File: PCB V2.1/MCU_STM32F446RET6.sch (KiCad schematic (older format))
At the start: 35 parts, among them J1 20021121-00010C4LF, J2 0475890001-MicroUSBPort, SW1 B3U-1000P, U1 STM32F446RET6_-_TQFP64, X1 ABM3B8.000MHZB2T, X2 ABS07-32.768KHZ-9-T

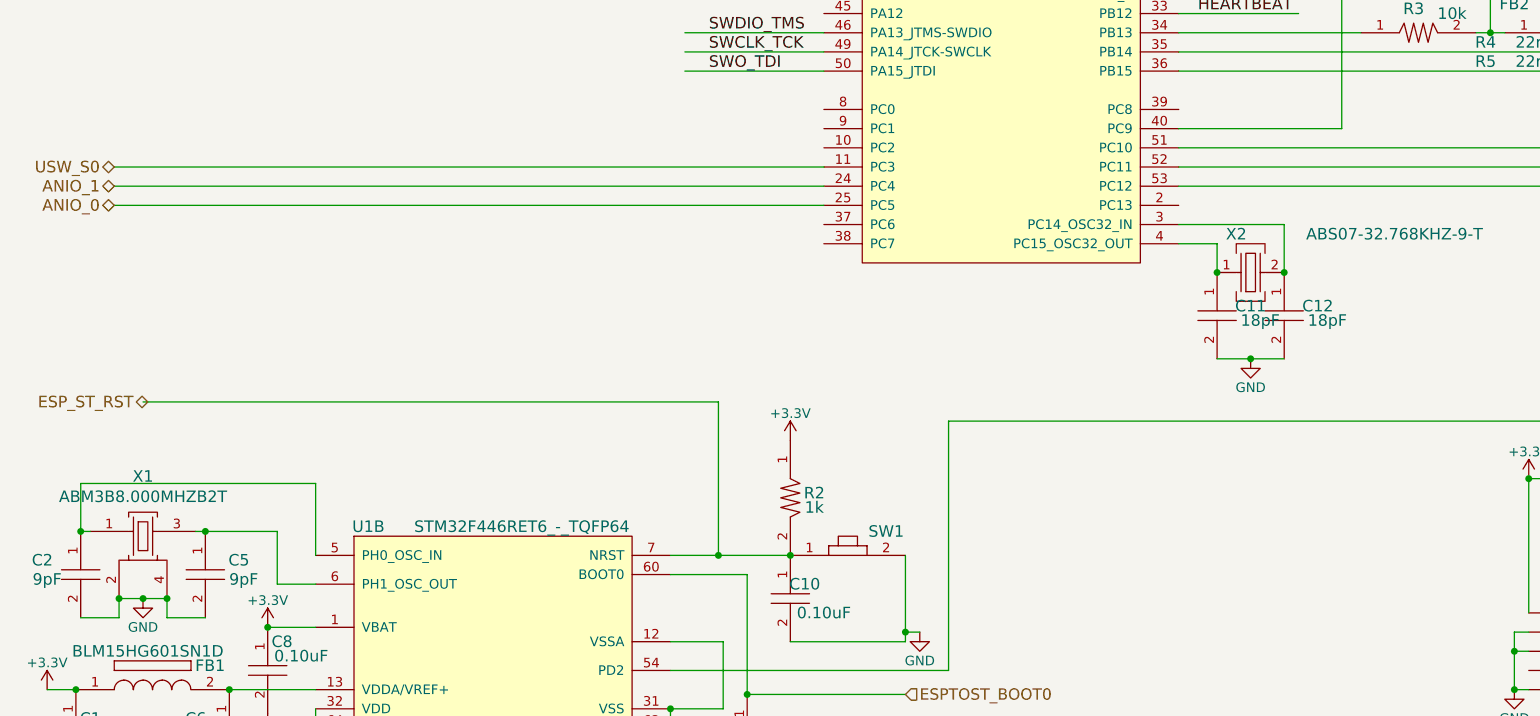
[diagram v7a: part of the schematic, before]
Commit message: Battery Monitoring & OTA
OTA signals between both processors solidified and routed. Battery
monitoring added as voltage divider into ADC channel. All but done
pending some small tweaks.
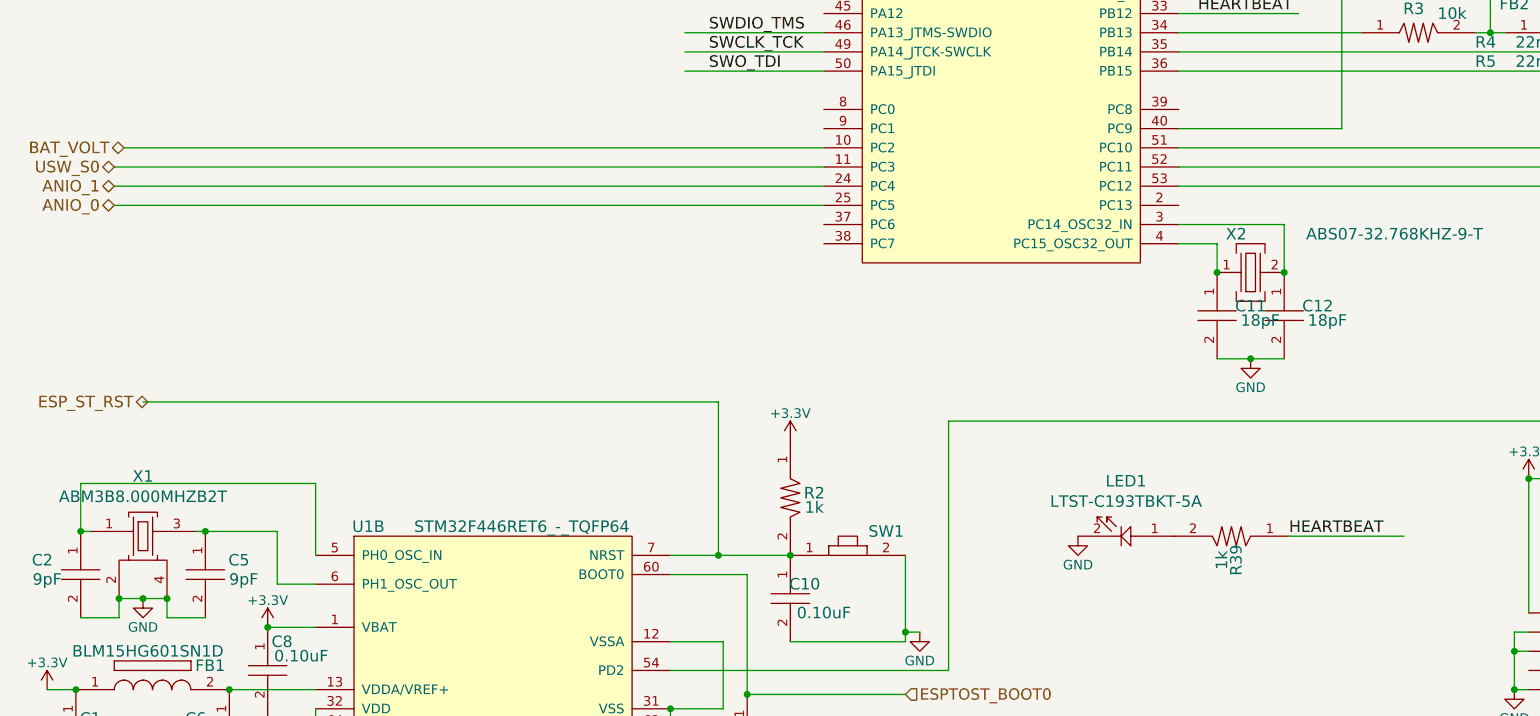
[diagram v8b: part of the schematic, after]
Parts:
- added LED1: LTST-C193TBKT-5A, PCB_Footprints:LED0603, symbol LTST-C193TBKT-5A
- added R39: RC1005F102CS, PCB_Footprints:R0402, symbol RC1005F102CS
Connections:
- net labels added: BAT_VOLT
- wire segments 120 -> 122
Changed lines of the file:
@@
 $EndComp
 $Comp
-L GND #PWR01
+L GND #PWR4
 U 1 1 57D43B63
 P 1125 6625
-F 0 "#PWR01" H 1125 6375 50  0001 C CNN
+F 0 "#PWR4" H 1125 6375 50  0001 C CNN
 F 1 "GND" H 1125 6475 50  0000 C CNN
 F 2 "" H 1125 6625 50  0000 C CNN
@@
 $EndComp
 $Comp
-L GND #PWR02
+L GND #PWR5
 U 1 1 57D43E04
 P 1450 7325
-F 0 "#PWR02" H 1450 7075 50  0001 C CNN
+F 0 "#PWR5" H 1450 7075 50  0001 C CNN
 F 1 "GND" H 1450 7175 50  0000 C CNN
 F 2 "" H 1450 7325 50  0000 C CNN
@@
 $EndComp
 $Comp
-L +3.3V #PWR03
+L +3.3V #PWR1
 U 1 1 57D443BB
 P 575 6175
-F 0 "#PWR03" H 575 6025 50  0001 C CNN
+F 0 "#PWR1" H 575 6025 50  0001 C CNN
 F 1 "+3.3V" H 575 6315 50  0000 C CNN
 F 2 "" H 575 6175 50  0000 C CNN
@@
 $EndComp
 $Comp
-L +3.3V #PWR04
+L +3.3V #PWR2
 U 1 1 57D444DD
 P 575 6875
-F 0 "#PWR04" H 575 6725 50  0001 C CNN
+F 0 "#PWR2" H 575 6725 50  0001 C CNN
 F 1 "+3.3V" H 575 7015 50  0000 C CNN
 F 2 "" H 575 6875 50  0000 C CNN
@@
 $EndComp
 $Comp
-L GND #PWR05
+L GND #PWR11
 U 1 1 57D449FF
 P 5125 5875
-F 0 "#PWR05" H 5125 5625 50  0001 C CNN
+F 0 "#PWR11" H 5125 5625 50  0001 C CNN
 F 1 "GND" H 5125 5725 50  0000 C CNN
 F 2 "" H 5125 5875 50  0000 C CNN
@@
 $EndComp
 $Comp
-L +3.3V #PWR06
+L +3.3V #PWR10
 U 1 1 57D45F91
 P 4450 4875
-F 0 "#PWR06" H 4450 4725 50  0001 C CNN
+F 0 "#PWR10" H 4450 4725 50  0001 C CNN
 F 1 "+3.3V" H 4450 5015 50  0000 C CNN
 F 2 "" H 4450 4875 50  0000 C CNN
@@
 $EndComp
 $Comp
-L GND #PWR07
+L GND #PWR8
 U 1 1 57D46AC6
 P 3825 7325
-F 0 "#PWR07" H 3825 7075 50  0001 C CNN
+F 0 "#PWR8" H 3825 7075 50  0001 C CNN
 F 1 "GND" H 3825 7175 50  0000 C CNN
 F 2 "" H 3825 7325 50  0000 C CNN
@@
 $EndComp
 $Comp
-L GND #PWR08
+L GND #PWR9
 U 1 1 57D47BC2
 P 4225 7325
-F 0 "#PWR08" H 4225 7075 50  0001 C CNN
+F 0 "#PWR9" H 4225 7075 50  0001 C CNN
 F 1 "GND" H 4225 7175 50  0000 C CNN
 F 2 "" H 4225 7325 50  0000 C CNN
@@
 $EndComp
 $Comp
-L GND #PWR09
+L GND #PWR3
 U 1 1 57D49635
 P 1075 5700
-F 0 "#PWR09" H 1075 5450 50  0001 C CNN
+F 0 "#PWR3" H 1075 5450 50  0001 C CNN
 F 1 "GND" H 1075 5550 50  0000 C CNN
 F 2 "" H 1075 5700 50  0000 C CNN
@@
 $EndComp
 $Comp
-L GND #PWR010
+L GND #PWR13
 U 1 1 57D4B2EA
 P 6850 4450
-F 0 "#PWR010" H 6850 4200 50  0001 C CNN
+F 0 "#PWR13" H 6850 4200 50  0001 C CNN
 F 1 "GND" H 6850 4300 50  0000 C CNN
 F 2 "" H 6850 4450 50  0000 C CNN
@@
 $EndComp
 $Comp
-L GND #PWR011
+L GND #PWR7
 U 1 1 57D4C07E
 P 1725 6300
-F 0 "#PWR011" H 1725 6050 50  0001 C CNN
+F 0 "#PWR7" H 1725 6050 50  0001 C CNN
 F 1 "GND" H 1725 6150 50  0000 C CNN
 F 2 "" H 1725 6300 50  0000 C CNN
@@
 $EndComp
 $Comp
-L GND #PWR012
+L GND #PWR16
 U 1 1 57D53F54
 P 8325 1150
-F 0 "#PWR012" H 8325 900 50  0001 C CNN
+F 0 "#PWR16" H 8325 900 50  0001 C CNN
 F 1 "GND" H 8325 1000 50  0000 C CNN
 F 2 "" H 8325 1150 50  0000 C CNN
@@
 $EndComp
 $Comp
-L GND #PWR013
+L GND #PWR20
 U 1 1 57D5C6D5
 P 10225 4150
-F 0 "#PWR013" H 10225 3900 50  0001 C CNN
+F 0 "#PWR20" H 10225 3900 50  0001 C CNN
 F 1 "GND" H 10225 4000 50  0000 C CNN
 F 2 "" H 10225 4150 50  0000 C CNN
@@
 $EndComp
 $Comp
-L GND #PWR014
+L GND #PWR18
 U 1 1 57D5C856
 P 9525 4250
-F 0 "#PWR014" H 9525 4000 50  0001 C CNN
+F 0 "#PWR18" H 9525 4000 50  0001 C CNN
 F 1 "GND" H 9525 4100 50  0000 C CNN
 F 2 "" H 9525 4250 50  0000 C CNN
@@
 $EndComp
 $Comp
-L GND #PWR015
+L GND #PWR19
 U 1 1 57D5C8C7
 P 9725 3150
-F 0 "#PWR015" H 9725 2900 50  0001 C CNN
+F 0 "#PWR19" H 9725 2900 50  0001 C CNN
 F 1 "GND" H 9725 3000 50  0000 C CNN
 F 2 "" H 9725 3150 50  0000 C CNN
@@
 $EndComp
 $Comp
-L GND #PWR016
+L GND #PWR17
 U 1 1 57D5FF55
 P 9125 3500
-F 0 "#PWR016" H 9125 3250 50  0001 C CNN
+F 0 "#PWR17" H 9125 3250 50  0001 C CNN
 F 1 "GND" H 9125 3350 50  0000 C CNN
 F 2 "" H 9125 3500 50  0000 C CNN
@@
 $EndComp
 $Comp
-L +3.3V #PWR017
+L +3.3V #PWR15
 U 1 1 57D61D70
 P 8300 5075
-F 0 "#PWR017" H 8300 4925 50  0001 C CNN
+F 0 "#PWR15" H 8300 4925 50  0001 C CNN
 F 1 "+3.3V" H 8300 5215 50  0000 C CNN
 F 2 "" H 8300 5075 50  0000 C CNN
@@
 Connection ~ 9725 3150
 $Comp
-L +3.3V #PWR018
+L +3.3V #PWR6
 U 1 1 57D91770
 P 1725 5850
-F 0 "#PWR018" H 1725 5700 50  0001 C CNN
+F 0 "#PWR6" H 1725 5700 50  0001 C CNN
 F 1 "+3.3V" H 1725 5990 50  0000 C CNN
 F 2 "" H 1725 5850 50  0000 C CNN
@@
 $EndComp
 $Comp
-L GND #PWR019
+L GND #PWR14
 U 1 1 57DDB978
 P 8225 6175
-F 0 "#PWR019" H 8225 5925 50  0001 C CNN
+F 0 "#PWR14" H 8225 5925 50  0001 C CNN
 F 1 "GND" H 8225 6025 50  0000 C CNN
 F 2 "" H 8225 6175 50  0000 C CNN
@@
 Wire Wire Line
 	10225 1650 6475 1650
+Text HLabel 975  3350 0    60   BiDi ~ 0
+BAT_VOLT
+Wire Wire Line
+	4625 3350 975  3350
+$Comp
+L LTST-C193TBKT-5A LED1
+U 1 1 57E101DC
+P 6200 5375
+F 0 "LED1" H 6200 5088 60  0000 C CNN
+F 1 "LTST-C193TBKT-5A" H 6200 5194 60  0000 C CNN
+F 2 "PCB_Footprints:LED0603" H 7625 7300 60  0001 C CNN
+F 3 "http://optoelectronics.liteon.com/upload/download/DS22-2004-060/P_100_LTST-C193TBKT-5A.pdf" H 7825 7425 60  0001 C CNN
+F 4 "0.06102 @ 6000" H 6050 5575 60  0001 C CNN "Cost"
+F 5 "8 Sept 2016" H 6150 5675 60  0001 C CNN "Date Created"
+F 6 "8 Sept 2016" H 6250 5775 60  0001 C CNN "Date Modified"
+F 7 "Adam Vadala-Roth" H 6350 5875 60  0001 C CNN "Designer"
+F 8 "0.55mm" H 6450 5975 60  0001 C CNN "Height"
+F 9 "Yes" H 6550 6075 60  0001 C CNN "RhoS?"
+F 10 "Lite-On Inc" H 6650 6175 60  0001 C CNN "MFR"
+F 11 "LTST-C193TBKT-5A" H 6750 6275 60  0001 C CNN "MFR#"
+F 12 "SMT/SMD" H 6850 6375 60  0001 C CNN "Mounting"
+F 13 "2" H 6950 6475 60  0001 C CNN "Pin Count#"
+F 14 "Active" H 7050 6575 60  0001 C CNN "Status"
+F 15 "N/A" H 7150 6675 60  0001 C CNN "Tolerance"
+F 16 "0603 LED" H 7250 6775 60  0001 C CNN "Type"
+F 17 "2.8V Forward Voltage" H 7350 6875 60  0001 C CNN "Voltage"
+F 18 "N/A" H 7450 6975 60  0001 C CNN "Wattage"
+F 19 "N/A" H 7550 7075 60  0001 C CNN "Component-Value"
+F 20 "Blue 470nm LED Indication - Discrete 2.8V 0603 (1608 Metric)" H 7650 7175 60  0001 C CNN "Description"
+	1    6200 5375
+	-1   0    0    1
+$EndComp
+$Comp
+L RC1005F102CS R39
+U 1 1 57E108CB
+P 6750 5375
+F 0 "R39" V 6725 5500 60  0000 C CNN
+F 1 "RC1005F102CS" H 6750 5225 60  0001 C CNN
+F 2 "PCB_Footprints:R0402" H 6350 5625 60  0001 C CNN
+F 3 "https://media.digikey.com/pdf/Data%20Sheets/Samsung%20PDFs/RC_Series_ds.pdf" H 6450 5825 60  0001 C CNN
+F 4 "0.00173 @ 5000" H 8300 7325 60  0001 C CNN "Cost"
+F 5 "5 Sept 2016" H 6650 5925 60  0001 C CNN "Date Created"
+F 6 "5 Sept 2016" H 6750 6025 60  0001 C CNN "Date Modified"
+F 7 "Adam Vadala-Roth" H 6850 6125 60  0001 C CNN "Designer"
+F 8 "0.4mm" H 6950 6225 60  0001 C CNN "Height"
+F 9 "Yes" H 7050 6325 60  0001 C CNN "RHoS?"
+F 10 "Samsung Electro-Mechanics America, Inc." H 7150 6425 60  0001 C CNN "MFR"
+F 11 "RC1005F102CS" H 7250 6525 60  0001 C CNN "MFR#"
+F 12 "SMT/SMD" H 7350 6625 60  0001 C CNN "Mounting"
+F 13 "2" H 7450 6725 60  0001 C CNN "Pin Count#"
+F 14 "Active" H 7550 6825 60  0001 C CNN "Status"
+F 15 "%" H 7650 6925 60  0001 C CNN "Tolerance"
+F 16 "passive" H 7750 7025 60  0001 C CNN "Type"
+F 17 "N/A" H 7850 7125 60  0001 C CNN "Voltage"
+F 18 "1/16" H 7950 7225 60  0001 C CNN "Wattage"
+F 19 "1k" V 6800 5500 60  0000 C CNN "Component-Value"
+F 20 "RES SMD 1K OHM 1% 1/16W 0402" H 8150 7425 60  0001 C CNN "Description"
+	1    6750 5375
+	-1   0    0    1
+$EndComp
+Text Label 7050 5375 0    60   ~ 0
+HEARTBEAT
+Wire Wire Line
+	7050 5375 7650 5375
+$Comp
+L GND #PWR12
+U 1 1 57E11BCD
+P 5950 5375
+F 0 "#PWR12" H 5950 5125 50  0001 C CNN
+F 1 "GND" H 5950 5225 50  0000 C CNN
+F 2 "" H 5950 5375 50  0000 C CNN
+F 3 "" H 5950 5375 50  0000 C CNN
+	1    5950 5375
+	1    0    0    -1
+$EndComp
 $EndSCHEMATC
